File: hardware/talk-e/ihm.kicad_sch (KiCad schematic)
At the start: 29 parts, among them J1 Conn_01x04_Socket, J2 Conn_01x02_Socket, J3 Conn_02x04_Odd_Even, J4 Conn_Coaxial, Q2 BC337, SW1 SW_Push, SW2 SW_Push, SW3 SW_Push, U1 RFM96W-433S2, U4 ESP32-S3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

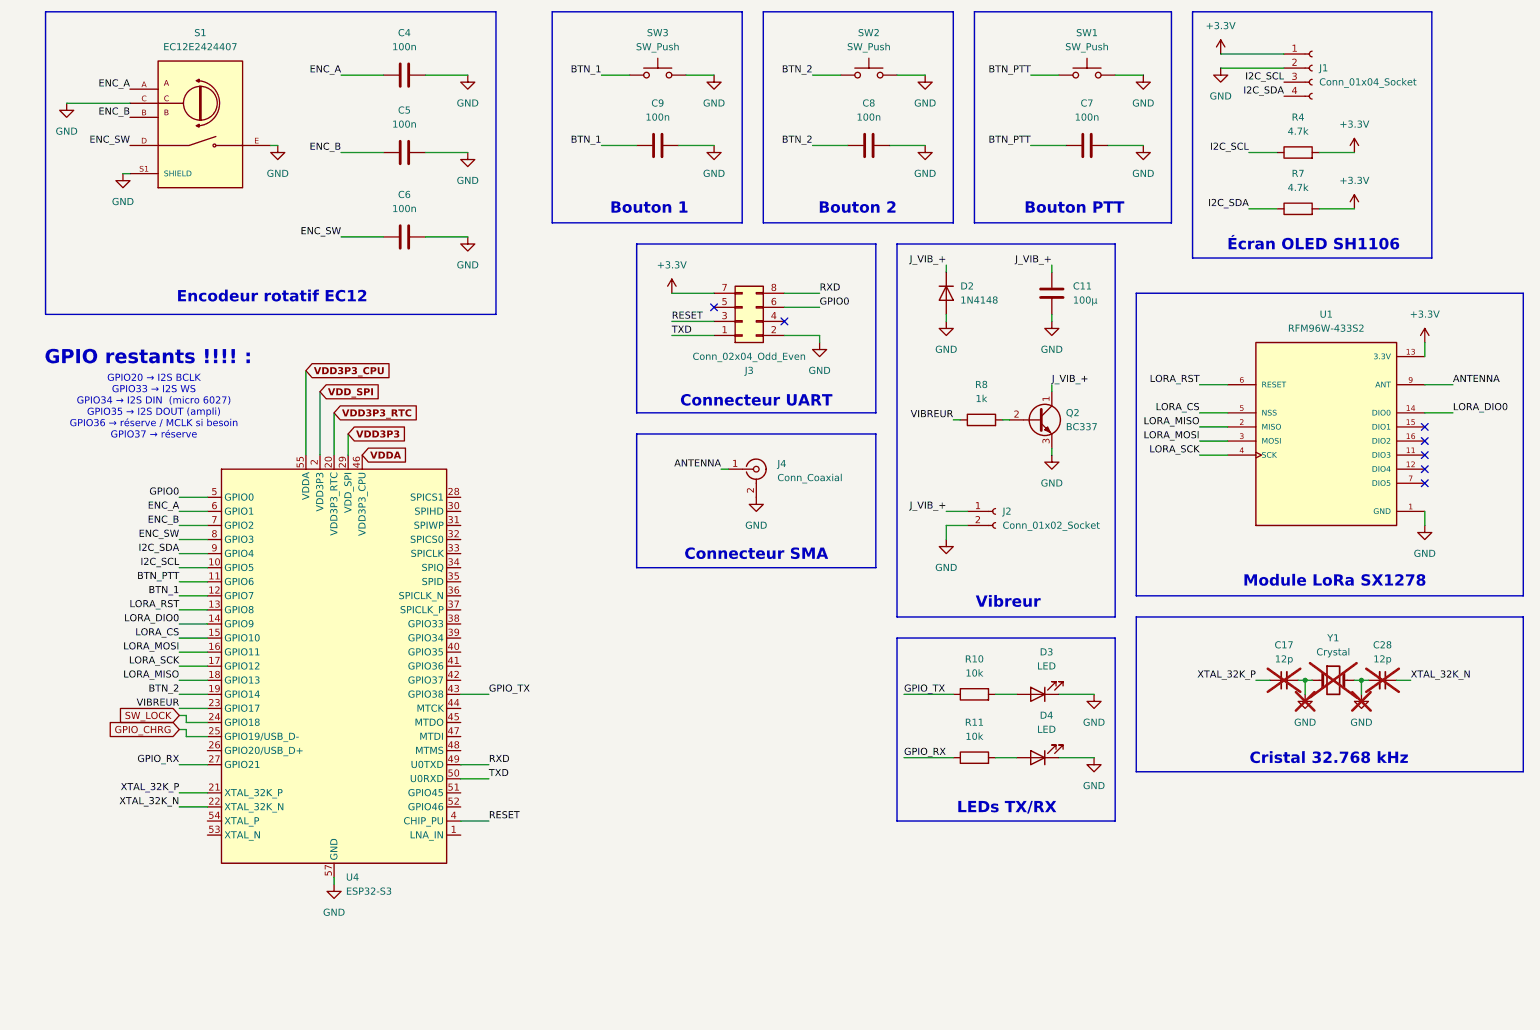
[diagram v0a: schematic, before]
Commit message: Added ampli + mic + finished GPIO mapping
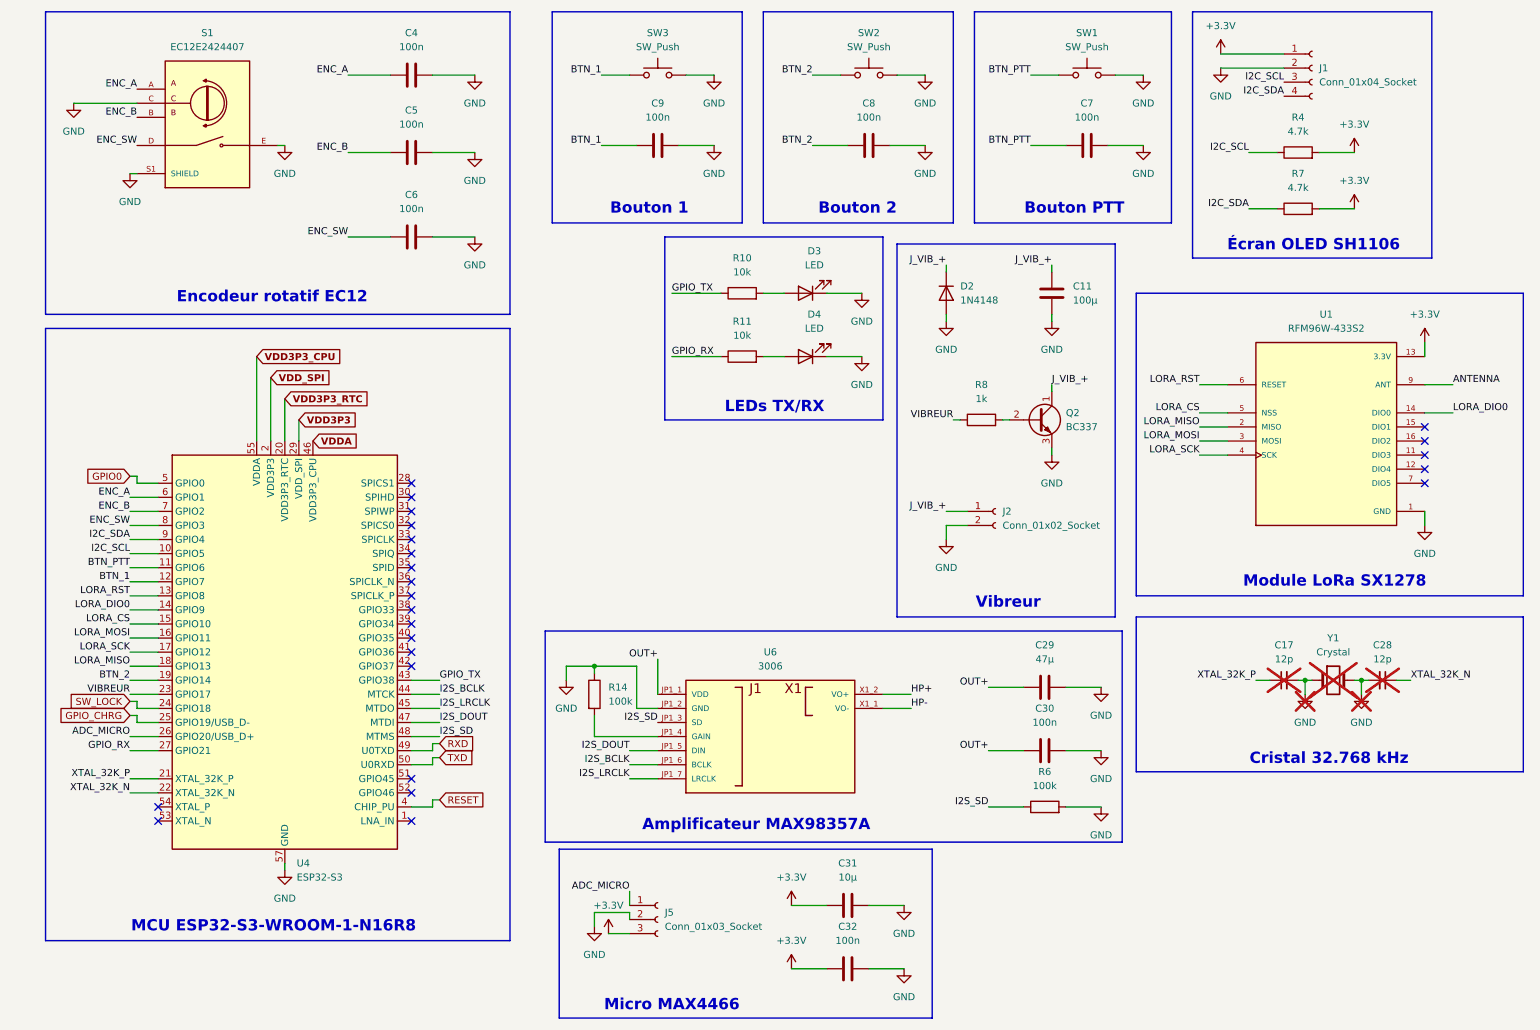
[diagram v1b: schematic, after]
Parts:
- removed J3: Conn_02x04_Odd_Even, Connector_IDC:IDC-Header_2x04_P2.54mm_Vertical, symbol Connector_Generic:Conn_02x04_Odd_Even
- removed J4: Conn_Coaxial, Connector_Coaxial:SMA_Amphenol_901-143_Horizontal, symbol Connector:Conn_Coaxial
- added C29: 47µ, symbol Device:C
- added C30, C32: 100n, symbol Device:C
- added C31: 10µ, symbol Device:C
- added J5: Conn_01x03_Socket, symbol Connector:Conn_01x03_Socket
- added R14, R6: 100k, symbol Device:R
- added U6: 3006, 3006:MODULE_3006, symbol 3006:3006
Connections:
- net +3.3V: now also C31.1, C32.1, J5.3 (Pin_3)
- net GND: now also C29.2, C30.2, C31.2, C32.2, J5.2 (Pin_2), R14.1, R6.2, U6.JP1_2 (GND)
- net ADC_MICRO: now reaches U4.26 (GPIO20/USB_D+)
- net ADC_MICRO: now also J5.1 (Pin_1)
- net I2S_BCLK: now reaches U4.44 (MTCK)
- net I2S_BCLK: now also U6.JP1_6 (BCLK)
- net I2S_LRCLK: now reaches U4.45 (MTDO)
- net I2S_LRCLK: now also U6.JP1_7 (LRCLK)
- net I2S_DOUT: now reaches U4.47 (MTDI)
- net I2S_DOUT: now also U6.JP1_5 (DIN)
- net I2S_SD: now reaches U4.48 (MTMS)
- net I2S_SD: now also R6.1, U6.JP1_3 (SD)
- new net: R14.2, U6.JP1_4 (GAIN)
- new net HP+: U6.X1_2 (VO+)
- new net HP-: U6.X1_1 (VO-)
- new net OUT+: C29.1, C30.1, U6.JP1_1 (VDD)
- no-connect marks 7 -> 24
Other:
- note added: "Amplificateur MAX98357A"
- note added: "MCU ESP32-S3-WROOM-1-N16R8"
- note added: "Micro MAX4466"
- note removed: "Connecteur SMA"
- note removed: "Connecteur UART"
- note removed: "GPIO restants !!!! :"
- note removed: "GPIO20 → I2S BCLK GPIO33 → I2S WS GPIO34 → I2S DIN (micro 6027) GPIO35 → I2S DOUT (ampli) GPIO36 → réserve / MCLK si besoin GPIO37 → réserve"
- moved on the sheet: C4, C5, C6, D3, D4, R10, R11, S1, U4

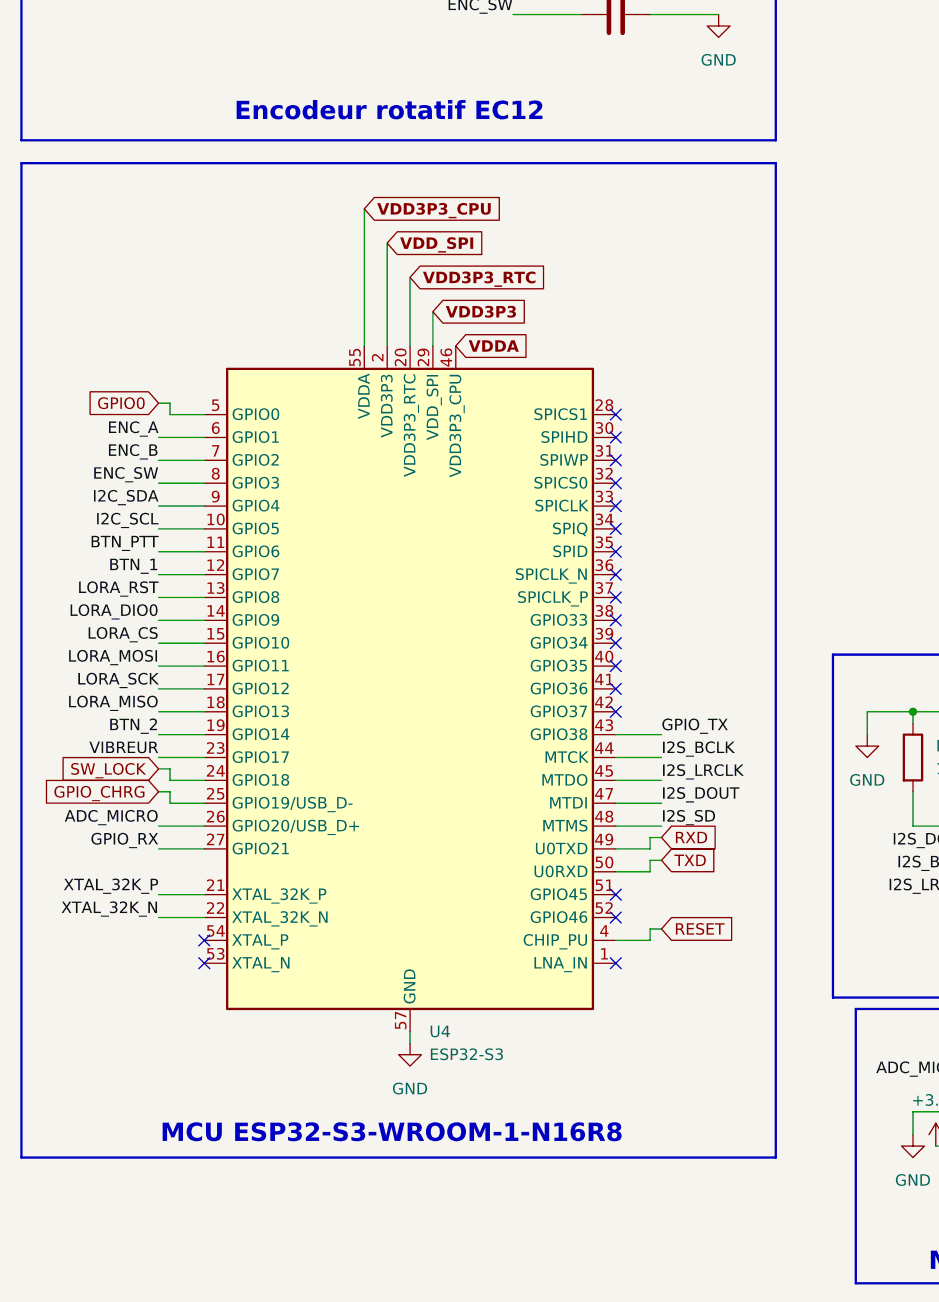
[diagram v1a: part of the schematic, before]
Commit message: Replaced ESP32-S3 with ESP32-S3-WROOM-1
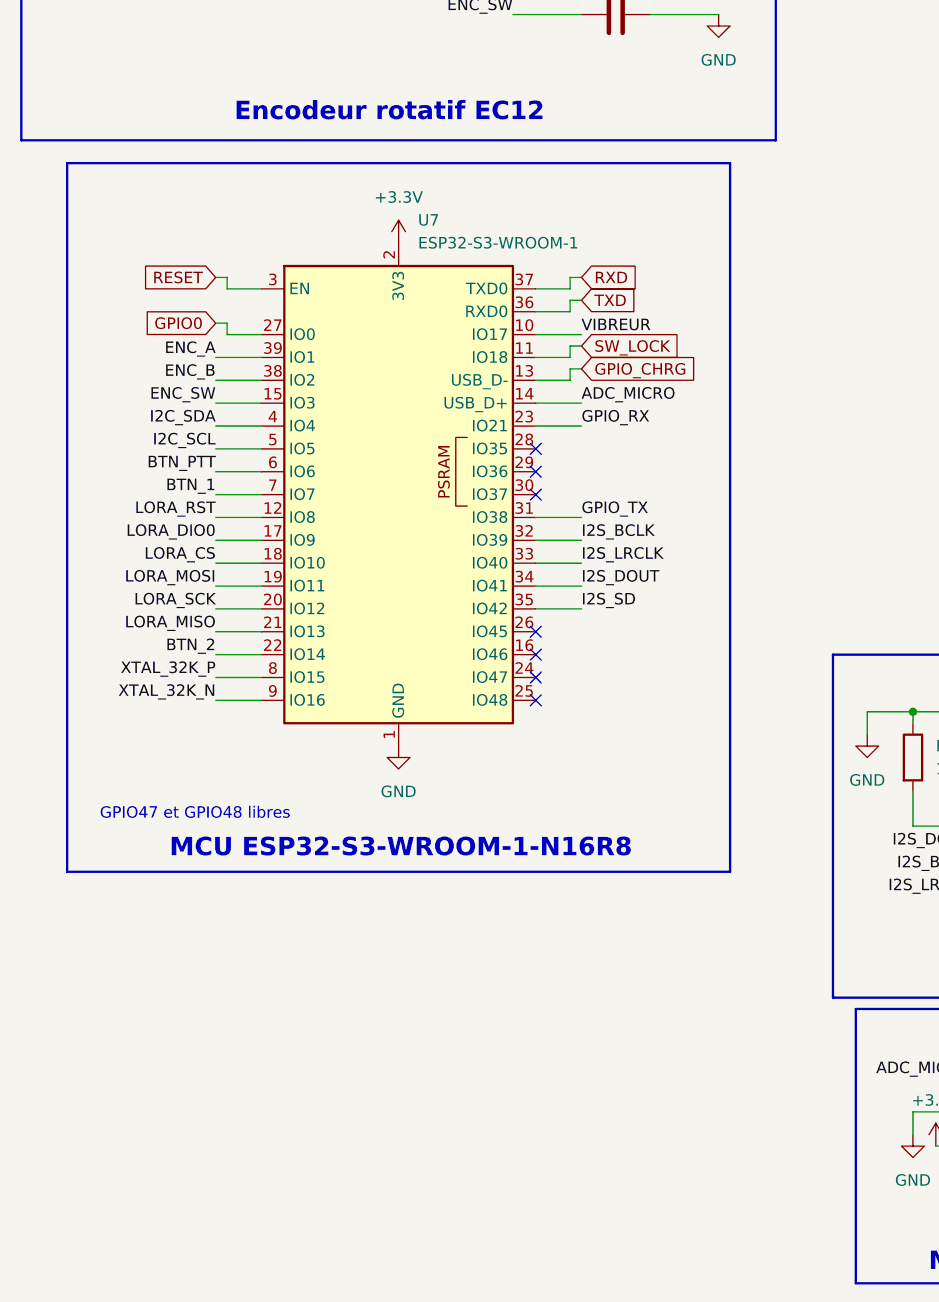
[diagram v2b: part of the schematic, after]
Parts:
- removed U4: ESP32-S3, Package_DFN_QFN:QFN-56-1EP_7x7mm_P0.4mm_EP4x4mm, symbol MCU_Espressif:ESP32-S3
- added U7: ESP32-S3-WROOM-1, RF_Module:ESP32-S3-WROOM-1, symbol RF_Module:ESP32-S3-WROOM-1
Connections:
- net +3.3V: now also U7.2 (3V3)
- net ADC_MICRO: now also U7.14 (USB_D+)
- net BTN_1: now also U7.7 (IO7)
- net BTN_2: now also U7.22 (IO14)
- net BTN_PTT: now also U7.6 (IO6)
- net ENC_A: now also U7.39 (IO1)
- net ENC_B: now also U7.38 (IO2)
- net ENC_SW: now also U7.15 (IO3)
- net GND: now also U7.1 (GND), U7.40 (GND), U7.41 (GND)
- net GPIO0: now also U7.27 (IO0)
- net GPIO_CHRG: now also U7.13 (USB_D-)
- net GPIO_RX: now also U7.23 (IO21)
- net GPIO_TX: now also U7.31 (IO38)
- net I2C_SCL: now also U7.5 (IO5)
- net I2C_SDA: now also U7.4 (IO4)
- net I2S_BCLK: now also U7.32 (IO39)
- net I2S_DOUT: now also U7.34 (IO41)
- net I2S_LRCLK: now also U7.33 (IO40)
- net I2S_SD: now also U7.35 (IO42)
- net LORA_CS: now also U7.18 (IO10)
- net LORA_DIO0: now also U7.17 (IO9)
- net LORA_MISO: now also U7.21 (IO13)
- net LORA_MOSI: now also U7.19 (IO11)
- net LORA_RST: now also U7.12 (IO8)
- net LORA_SCK: now also U7.20 (IO12)
- net RESET: now also U7.3 (EN)
- net RXD: now also U7.37 (TXD0)
- net SW_LOCK: now also U7.11 (IO18)
- net TXD: now also U7.36 (RXD0)
- net VIBREUR: now also U7.10 (IO17)
- net XTAL_32K_N: now also U7.9 (IO16)
- net XTAL_32K_P: now also U7.8 (IO15)
- no-connect marks 24 -> 12
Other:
- note added: "GPIO47 et GPIO48 libres"

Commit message: Finished routing + PCB ready for production
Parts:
- removed C17, C28: 12p, symbol Device:C_Small
- removed D3, D4: LED, symbol Device:LED
- removed R10, R11: 10k, symbol Device:R
- removed SW1, SW2, SW3: SW_Push, symbol Switch:SW_Push
- removed Y1: Crystal, symbol Device:Crystal
- added C20, C6: 100n, Capacitor_SMD:C_0805_2012Metric, symbol Device:C
- added C5: 10µ, Capacitor_SMD:C_0805_2012Metric, symbol Device:C
- added J10, J13, J5, J6, J7: Conn_01x02_Socket, Connector_JST:JST_EH_B2B-EH-A_1x02_P2.50mm_Vertical, symbol Connector:Conn_01x02_Socket
- added J4: Conn_01x04_Socket, Connector_JST:JST_EH_B4B-EH-A_1x04_P2.50mm_Vertical, symbol Connector:Conn_01x04_Socket
- added R5: 10k, Resistor_SMD:R_1206_3216Metric, symbol Device:R
- added R6, R7: 330R, Resistor_SMD:R_1206_3216Metric, symbol Device:R
- C1: renamed from C6; footprint (none) -> Capacitor_SMD:C_0805_2012Metric; KiLib_Generator (none) -> SMD_2terminal_chip_molded
- C17: renamed from C31; footprint (none) -> Capacitor_SMD:C_0805_2012Metric; KiLib_Generator (none) -> SMD_2terminal_chip_molded
- C18: renamed from C32; footprint (none) -> Capacitor_SMD:C_0805_2012Metric; KiLib_Generator (none) -> SMD_2terminal_chip_molded
- C2: renamed from C5; footprint (none) -> Capacitor_SMD:C_0805_2012Metric; KiLib_Generator (none) -> SMD_2terminal_chip_molded
- C23: renamed from C29; footprint (none) -> Capacitor_SMD:C_0805_2012Metric; KiLib_Generator (none) -> SMD_2terminal_chip_molded
- C24: renamed from C30; footprint (none) -> Capacitor_SMD:C_0805_2012Metric; KiLib_Generator (none) -> SMD_2terminal_chip_molded
- C3: renamed from C4; footprint (none) -> Capacitor_SMD:C_0805_2012Metric; KiLib_Generator (none) -> SMD_2terminal_chip_molded
- C4: renamed from C11; footprint (none) -> Capacitor_SMD:C_0805_2012Metric; KiLib_Generator (none) -> SMD_2terminal_chip_molded
- C7, C8, C9: footprint (none) -> Capacitor_SMD:C_0805_2012Metric; KiLib_Generator (none) -> SMD_2terminal_chip_molded
- D1: renamed from D2; KiLib_Generator (none) -> diode/THT
- J11: renamed from J5; footprint (none) -> Connector_JST:JST_EH_B3B-EH-A_1x03_P2.50mm_Vertical; KiLib_Generator (none) -> connector/JST
- J2: footprint Connector_JST:JST_EH_S2B-EH_1x02_P2.50mm_Horizontal -> Connector_JST:JST_EH_B2B-EH-A_1x02_P2.50mm_Vertical; KiLib_Generator (none) -> connector/JST
- J3: renamed from J1; footprint Connector_PinSocket_2.54mm:PinSocket_1x04_P2.54mm_Vertical -> Connector_JST:JST_EH_B4B-EH-A_1x04_P2.50mm_Vertical; KiLib_Generator (none) -> connector/JST
- R1: renamed from R4; footprint (none) -> Resistor_SMD:R_1206_3216Metric; KiLib_Generator (none) -> SMD_2terminal_chip_molded
- R17: renamed from R14; footprint (none) -> Resistor_SMD:R_1206_3216Metric; KiLib_Generator (none) -> SMD_2terminal_chip_molded
- R18: renamed from R6; footprint (none) -> Resistor_SMD:R_1206_3216Metric; KiLib_Generator (none) -> SMD_2terminal_chip_molded
- R2: renamed from R7; footprint (none) -> Resistor_SMD:R_1206_3216Metric; KiLib_Generator (none) -> SMD_2terminal_chip_molded
- R3: renamed from R8; footprint (none) -> Resistor_SMD:R_1206_3216Metric; KiLib_Generator (none) -> SMD_2terminal_chip_molded
- renumbered Q2 to Q1, U7 to U1, U1 to U6, U6 to U7
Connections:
- net +3.3V: now also C7.1, C20.1, C5.1, R5.2
- net BTN_1: now also J7.1 (Pin_1)
- net BTN_2: now also J6.1 (Pin_1)
- net BTN_PTT: now also C6.1, J5.1 (Pin_1); no longer C7.1
- net ENC_A: now also J4.1 (Pin_1)
- net ENC_B: now also J4.2 (Pin_2)
- net ENC_SW: now also J4.3 (Pin_3), R5.1
- net GND: now also C20.2, C5.2, C6.2, J10.2 (Pin_2), J13.2 (Pin_2), J4.4 (Pin_4), J5.2 (Pin_2), J6.2 (Pin_2), J7.2 (Pin_2)
- net GPIO_RX: now also R6.1
- net GPIO_TX: now also R7.1
- net XTAL_32K_N: no longer names the net of U1.9 (IO16)
- net XTAL_32K_P: no longer names the net of U1.8 (IO15)
- new net: J10.1 (Pin_1), R6.2
- new net: J13.1 (Pin_1), R7.2
- no-connect marks 12 -> 14
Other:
- note added: "Microphone MAX4466"
- note added: "Strapping pin JTAG"
- note removed: "Cristal 32.768 kHz"
- note removed: "Micro MAX4466"
- moved on the sheet: C17, C18, C23, C24, C4, C9, D1, J11, J2, J3, Q1, R1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
